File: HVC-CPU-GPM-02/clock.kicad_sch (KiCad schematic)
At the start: 13 parts, among them Q2 2SC2021, Y1 21.47727MHz

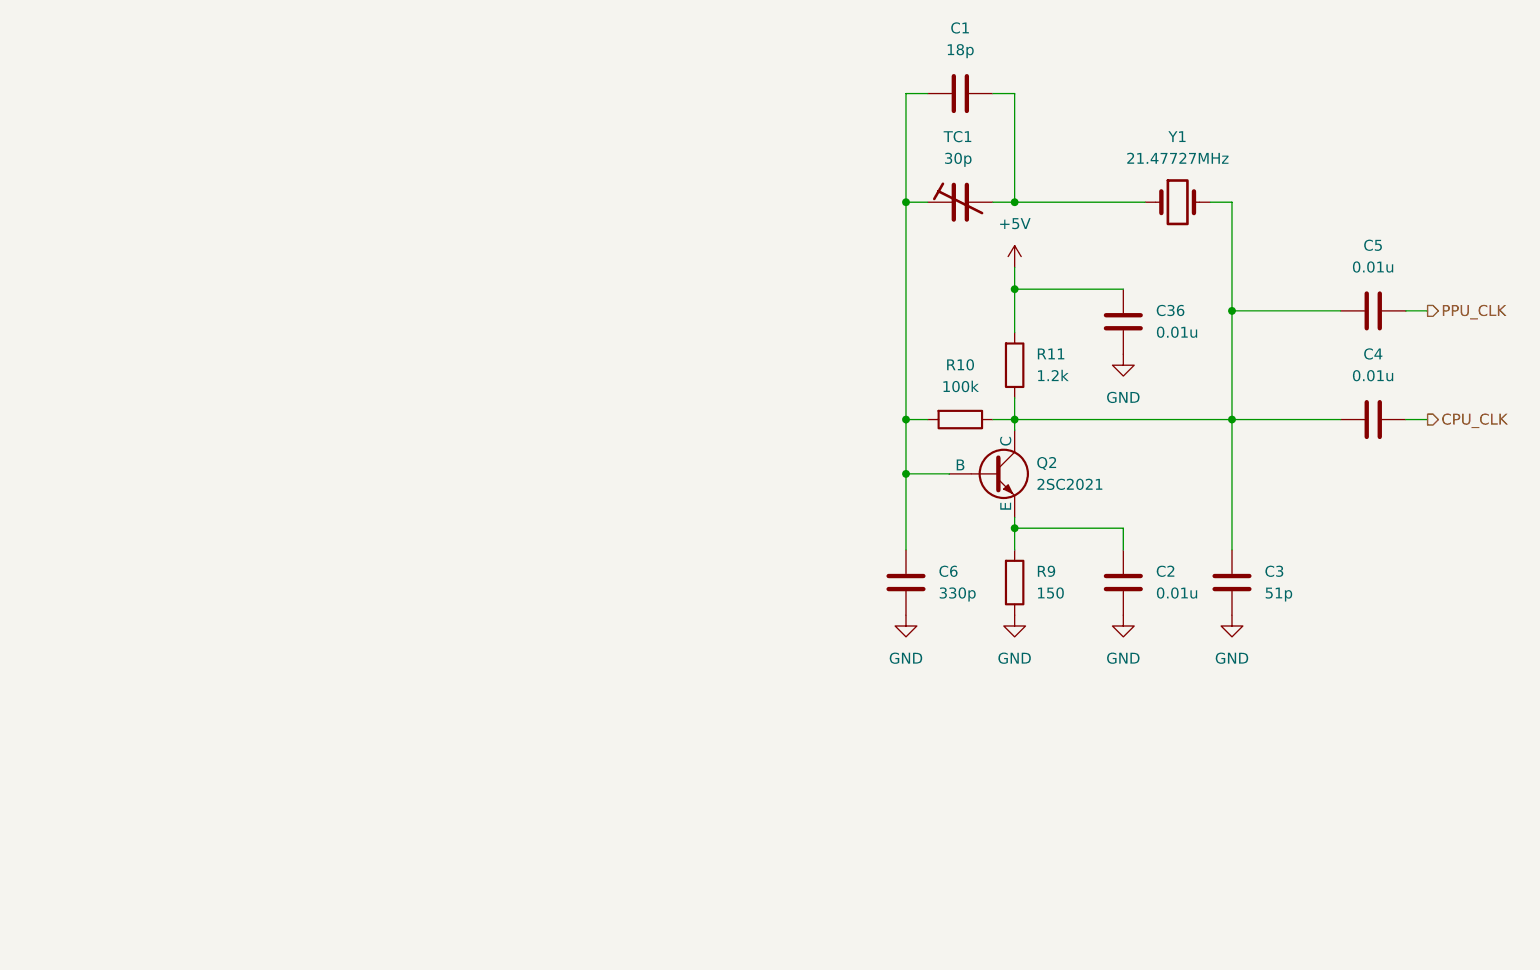
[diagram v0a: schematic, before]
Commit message: Refactor schematic: * Move audio and video circuits to dedicated sheet * Move power and mechanical to dedicated sheet Modify P1 Cart Connector symbol to: * split out audio ports * organize pins for easier wiring Modify 74LS346 symbol: * Split A/B ports to allow moving functions to related circuits Modify X1 crystal footprint: * change from stock footprint to custom footprint Correct crystal name from Y1 to X1
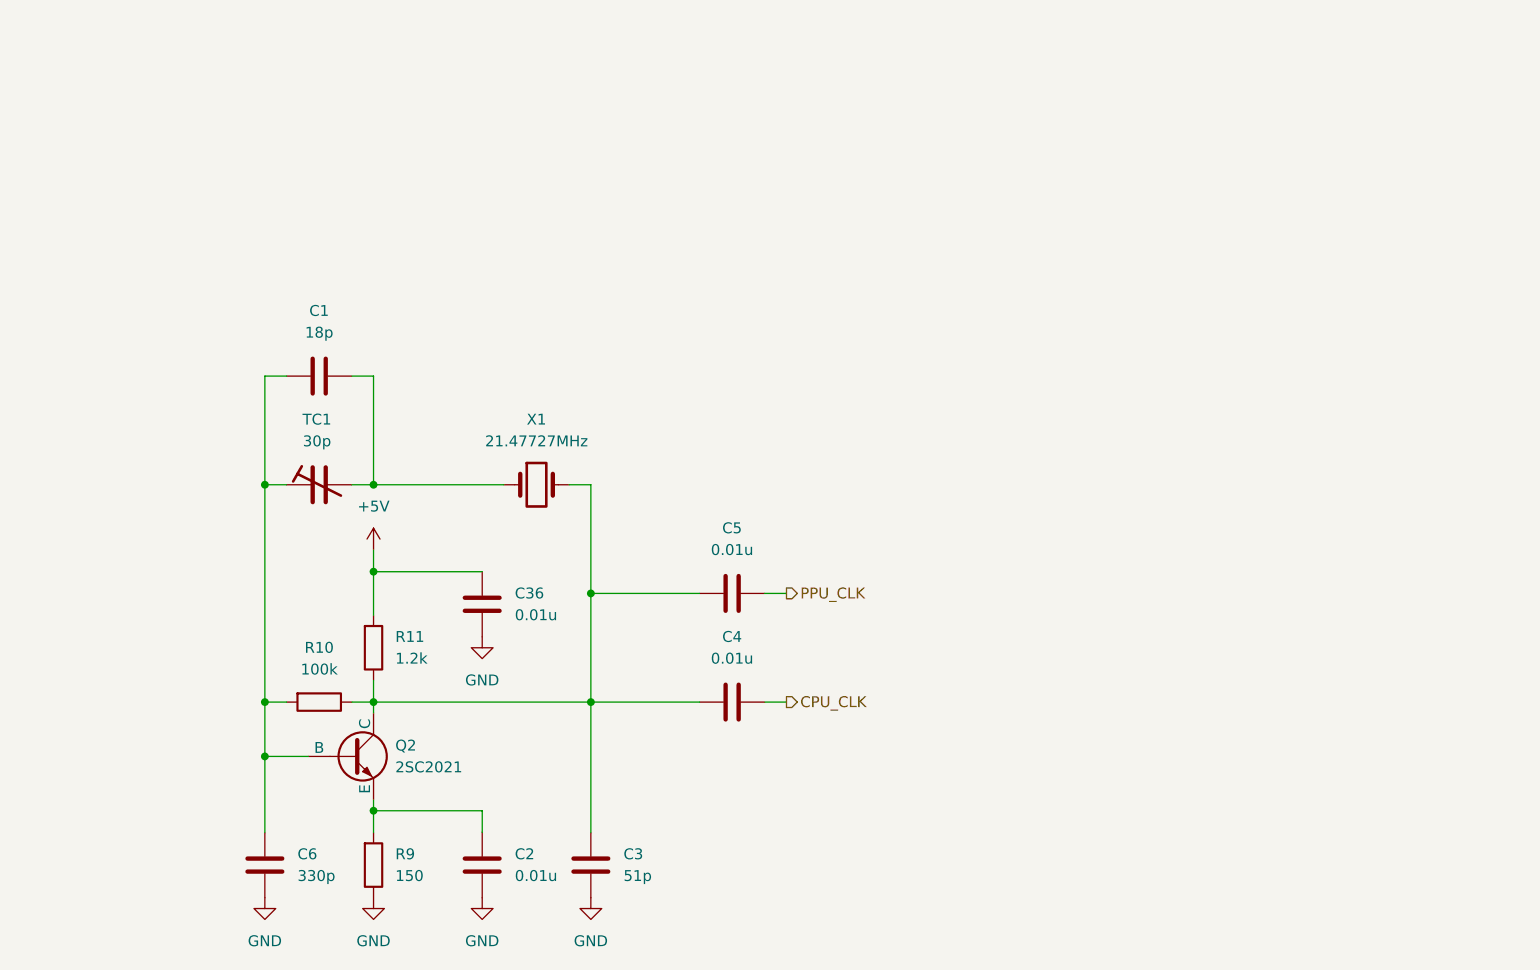
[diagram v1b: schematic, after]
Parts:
- X1: renamed from Y1; footprint Crystal:Crystal_HC49-4H_Vertical -> Nintendo:crystal
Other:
- moved on the sheet: C1, C2, C3, C36, C4, C5, C6, Q2, R10, R11, R9, TC1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

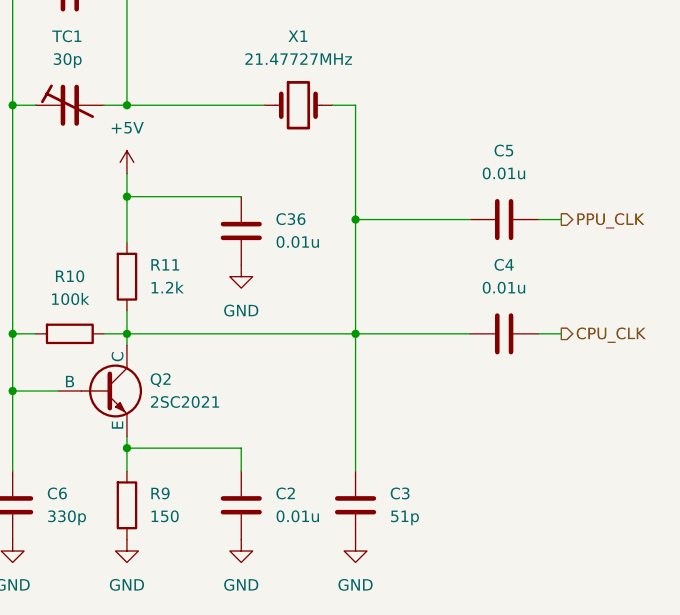
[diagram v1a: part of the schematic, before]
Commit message: Change symbols to functional layout instead of pin map layout Add technical page to store pinouts Organize and compact root page
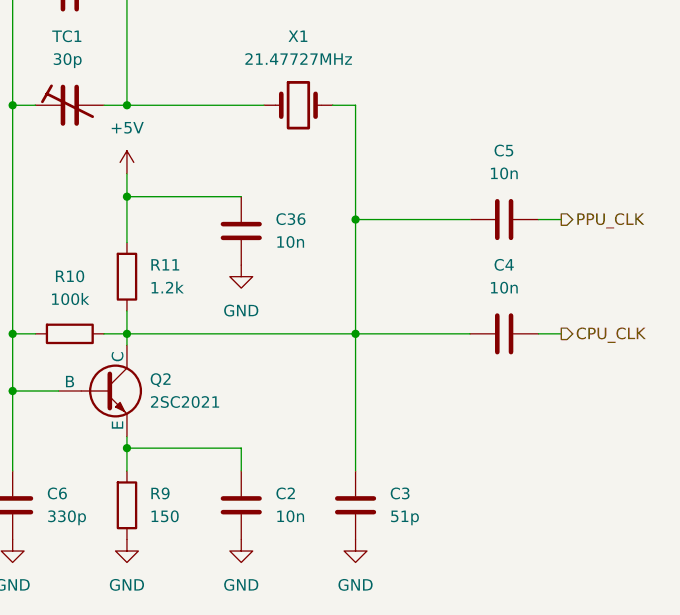
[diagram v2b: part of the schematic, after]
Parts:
- C2, C36, C4, C5: value 0.01u -> 10n
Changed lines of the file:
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@@
 			)
 		)
-		(property "Value" "0.01u"
+		(property "Value" "10n"
 			(at 106.68 129.5399 0)
 			(effects
@@
 			)
 		)
-		(property "Value" "0.01u"
+		(property "Value" "10n"
 			(at 132.08 91.44 90)
 			(effects
@@
 			)
 		)
-		(property "Value" "0.01u"
+		(property "Value" "10n"
 			(at 106.68 99.0599 0)
 			(effects
@@
 			)
 		)
-		(property "Value" "0.01u"
+		(property "Value" "10n"
 			(at 132.08 104.14 90)
 			(effects

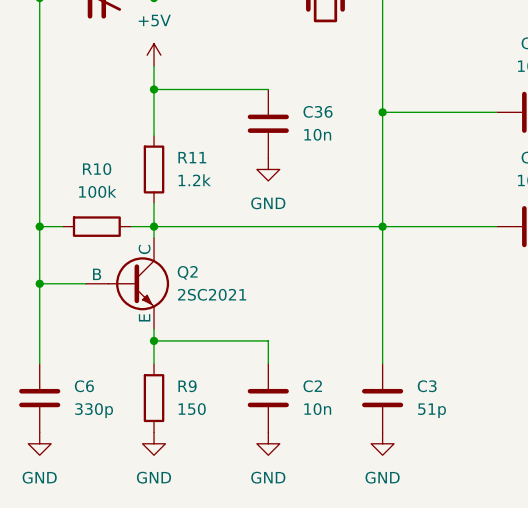
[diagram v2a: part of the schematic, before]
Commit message: Rearranged pins on some symbols to simplify schematic wiring Removed schematics for controller PCBs Added PNG version of schematics
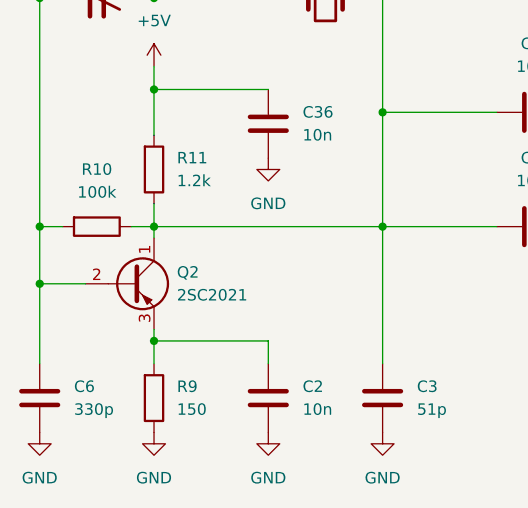
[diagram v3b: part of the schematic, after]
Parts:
- Q2: symbol Simulation_SPICE:NPN -> Transistor_BJT:Q_PNP_CBE
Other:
- title: (none) -> Nintendo Famicom Mainboard
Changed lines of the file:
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@@
 	(generator_version "9.0")
 	(paper "A4")
+	(title_block
+		(title "Nintendo Famicom Mainboard")
+		(date "2025-10-30")
+		(rev "1")
+	)
 	(junction
 		(at 77.47 83.82)
@@
 	)
 	(symbol
-		(lib_id "Simulation_SPICE:NPN")
+		(lib_id "Transistor_BJT:Q_PNP_CBE")
 		(at 87.63 115.57 0)
 		(unit 1)
@@
 		)
 		(property "Footprint" "Nintendo:PACKAGE_TRANSISTOR_FTR"
-			(at 151.13 115.57 0)
-			(effects
-				(font
-					(size 1.27 1.27)
-				)
-				(hide yes)
-			)
-		)
-		(property "Datasheet" "https://ngspice.sourceforge.io/docs/ngspice-html-manual/manual.xhtml#cha_BJTs"
-			(at 151.13 115.57 0)
-			(effects
-				(font
-					(size 1.27 1.27)
-				)
-				(hide yes)
-			)
-		)
-		(property "Description" "Bipolar transistor symbol for simulation only, substrate tied to the emitter"
+			(at 92.71 113.03 0)
+			(effects
+				(font
+					(size 1.27 1.27)
+				)
+				(hide yes)
+			)
+		)
+		(property "Datasheet" "~"
 			(at 87.63 115.57 0)
 			(effects
+				(font
+					(size 1.27 1.27)
+				)
+				(hide yes)
+			)
+		)
+		(property "Description" "PNP transistor, collector/base/emitter"
+			(at 87.63 115.57 0)
+			(effects

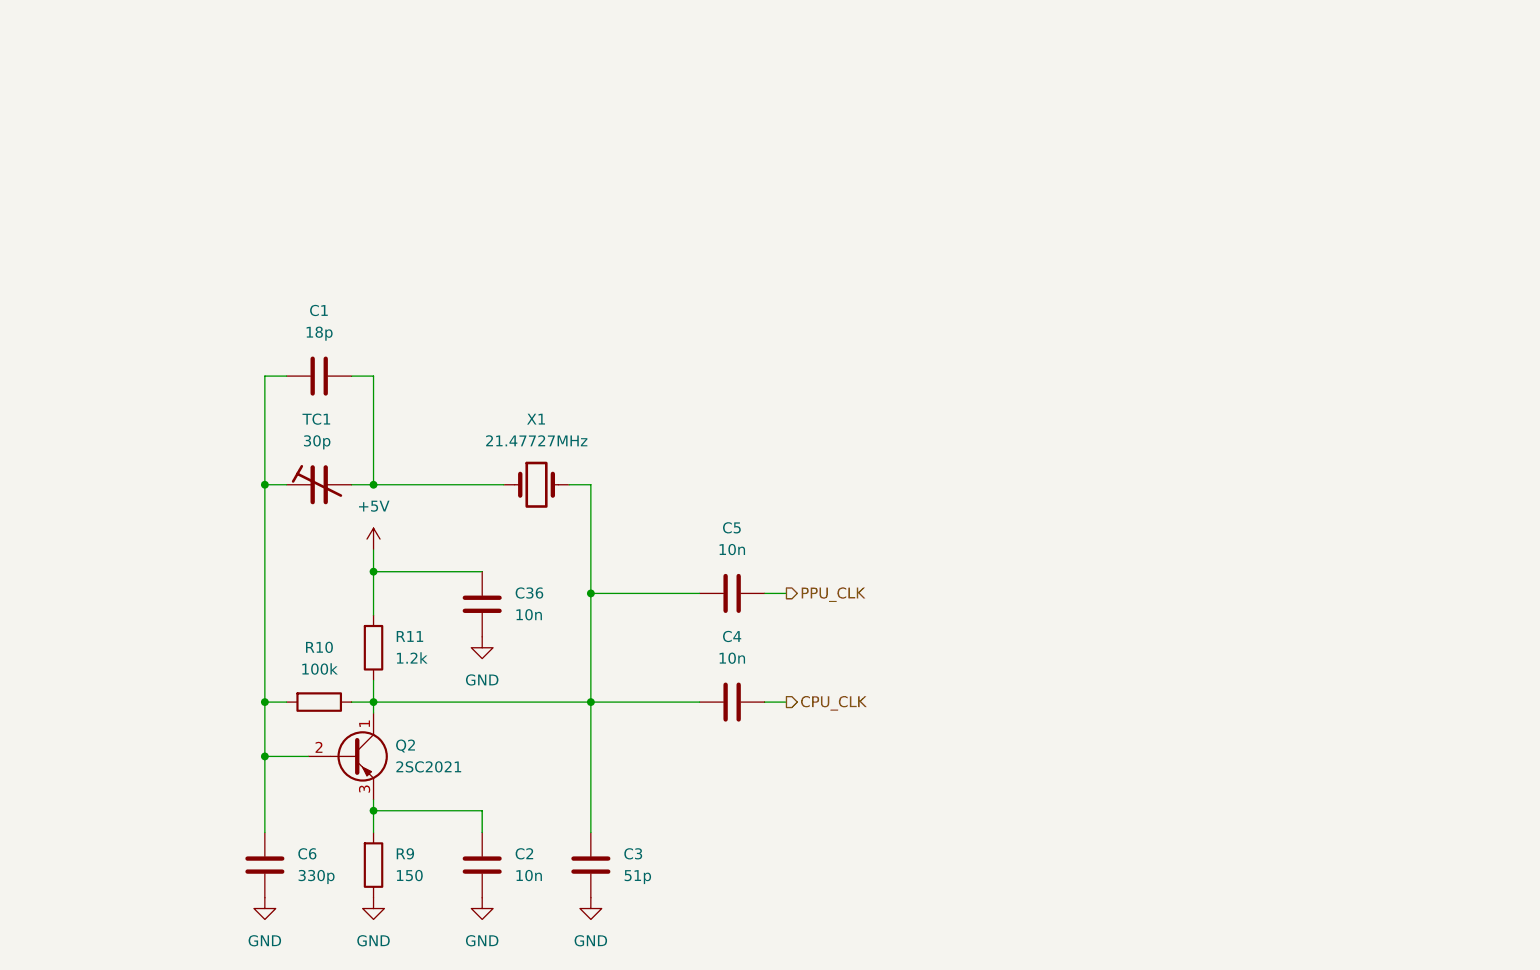
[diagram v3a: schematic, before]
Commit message: annotate schematics, correct PCB/schematic parity issure, add datasheets
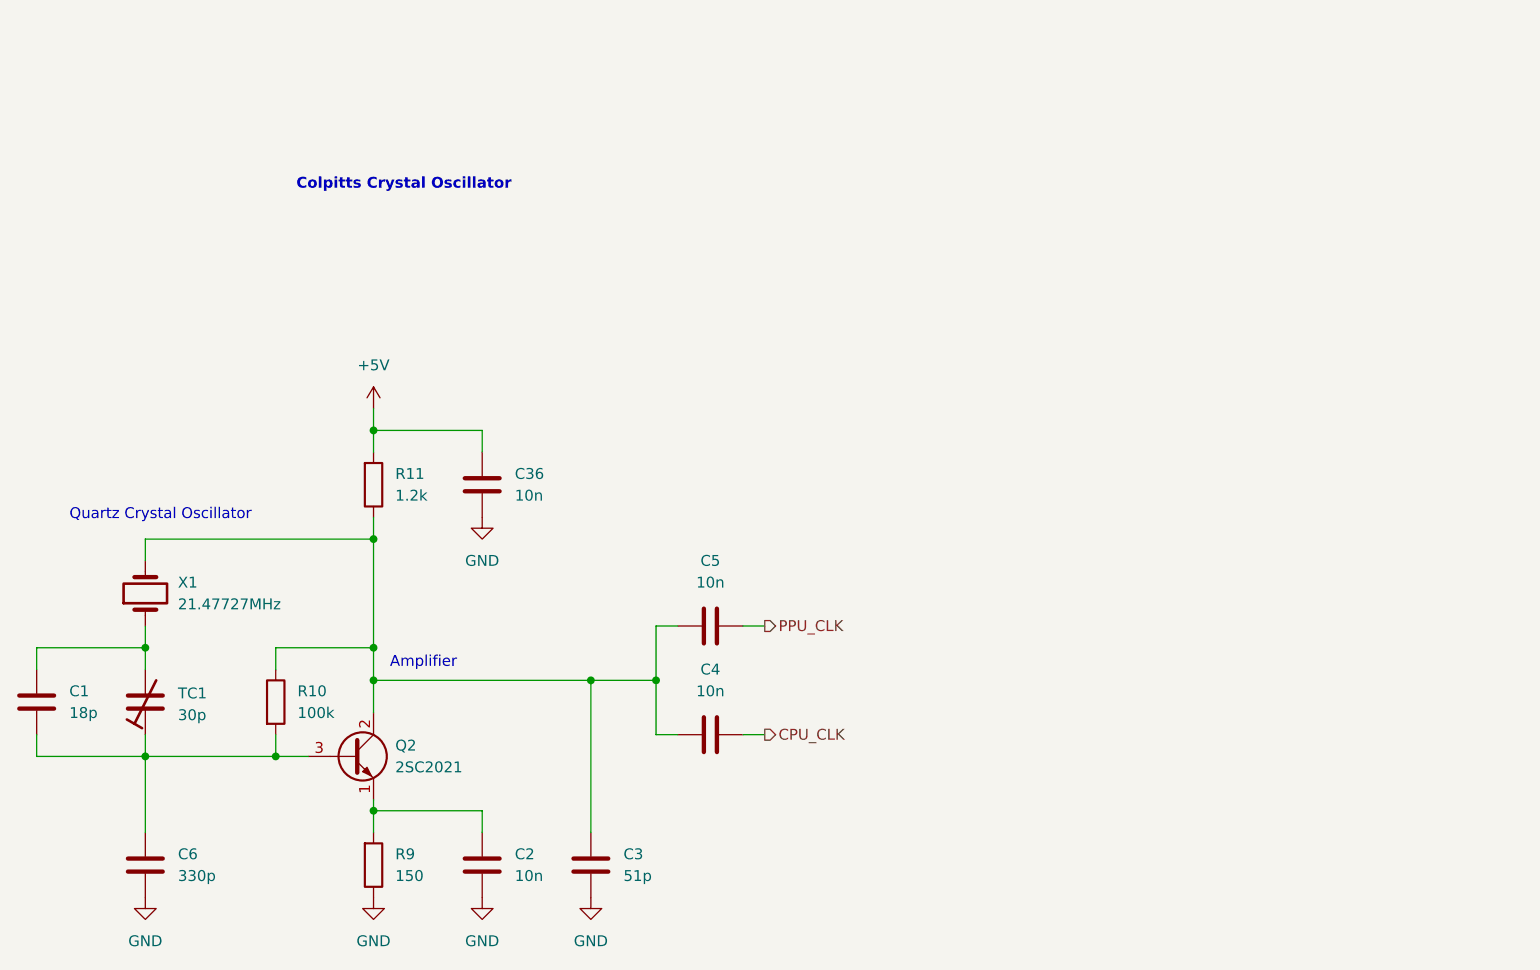
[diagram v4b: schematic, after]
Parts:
- C1, C2, C3, C36, C4, C5, C6: footprint Nintendo:C_Disc_D3.0mm_W2.0mm_P3.0mm -> Nintendo:C_Disc_NoSilk_D3.0mm_W2.0mm_P3.0mm
- Q2: symbol Transistor_BJT:Q_PNP_CBE -> Transistor_BJT:Q_NPN_ECB
- R10, R11, R9: footprint Resistor_THT:R_Axial_DIN0207_L6.3mm_D2.5mm_P10.16mm_Horizontal -> Nintendo:R_Axial_NoSilk_DIN0207_L6.3mm_D2.5mm_P10.16mm_Horizontal
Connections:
- net at C1.1, C6.2, R10.2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: now also Q2.3 (B); no longer Q2.2 (B)
- net at C2.2, R9.2: now also Q2.1 (E); no longer Q2.3 (E)
- net at C3.2, C4.2, C5.2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: now also Q2.2 (C); no longer Q2.1 (C)
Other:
- note added: "Amplifier"
- note added: "Colpitts Crystal Oscillator"
- note added: "Quartz Crystal Oscillator"
- moved on the sheet: C1, C36, C4, C5, C6, R10, R11, TC1, X1

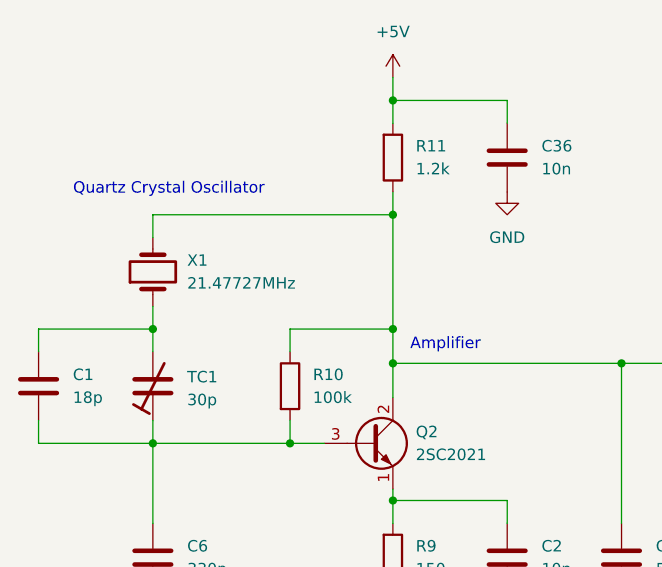
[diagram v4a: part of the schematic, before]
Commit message: Updated PCB and footprints to correct hole and pad sizes
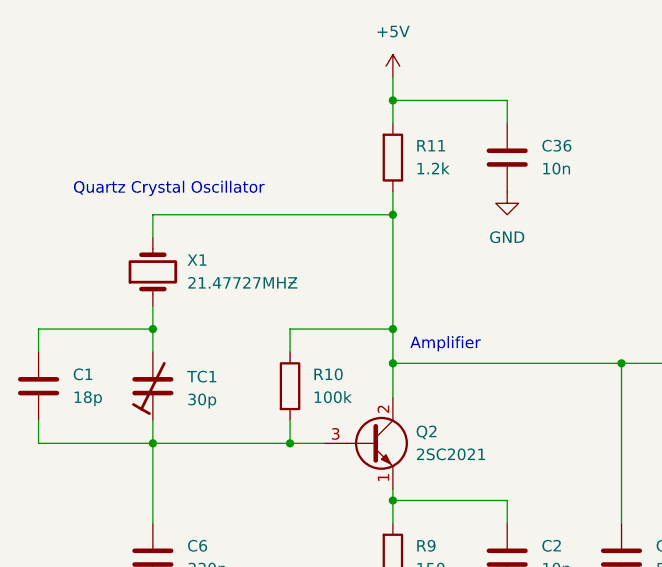
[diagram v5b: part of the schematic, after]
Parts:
- X1: value 21.47727MHz -> 21.47727MHƵ
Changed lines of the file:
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@@
 			)
 		)
-		(property "Value" "21.47727MHz"
+		(property "Value" "21.47727MHƵ"
 			(at 67.31 97.7899 90)
 			(effects
